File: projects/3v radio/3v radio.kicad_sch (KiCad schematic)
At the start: 6 parts

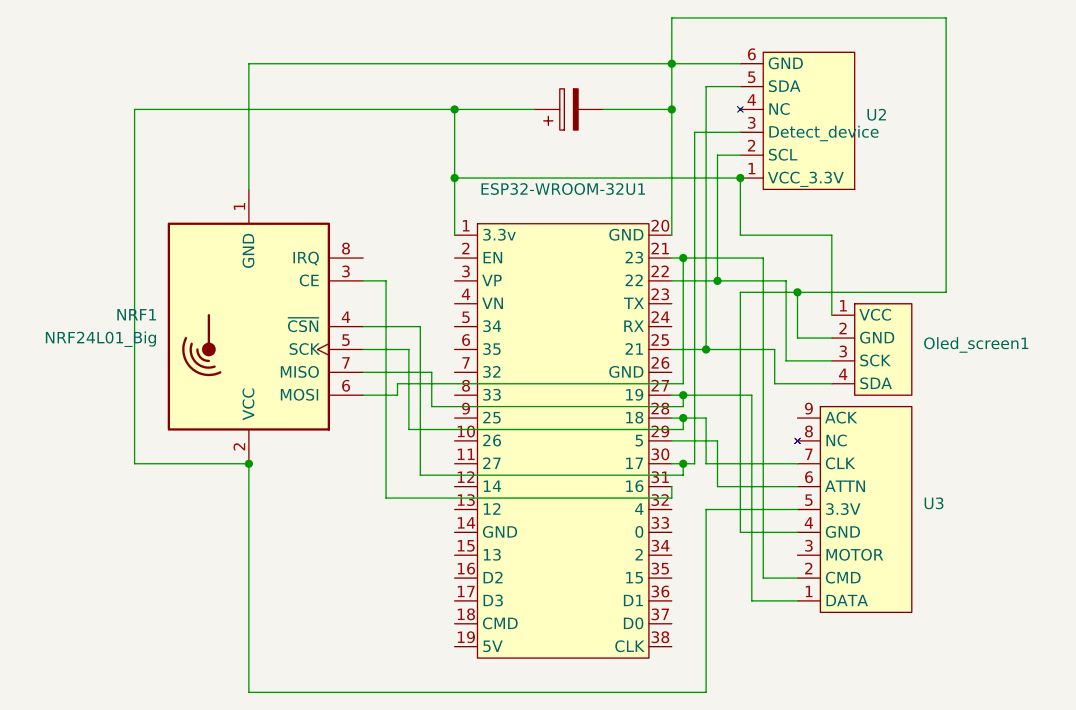
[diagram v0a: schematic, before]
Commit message: 3v rad update
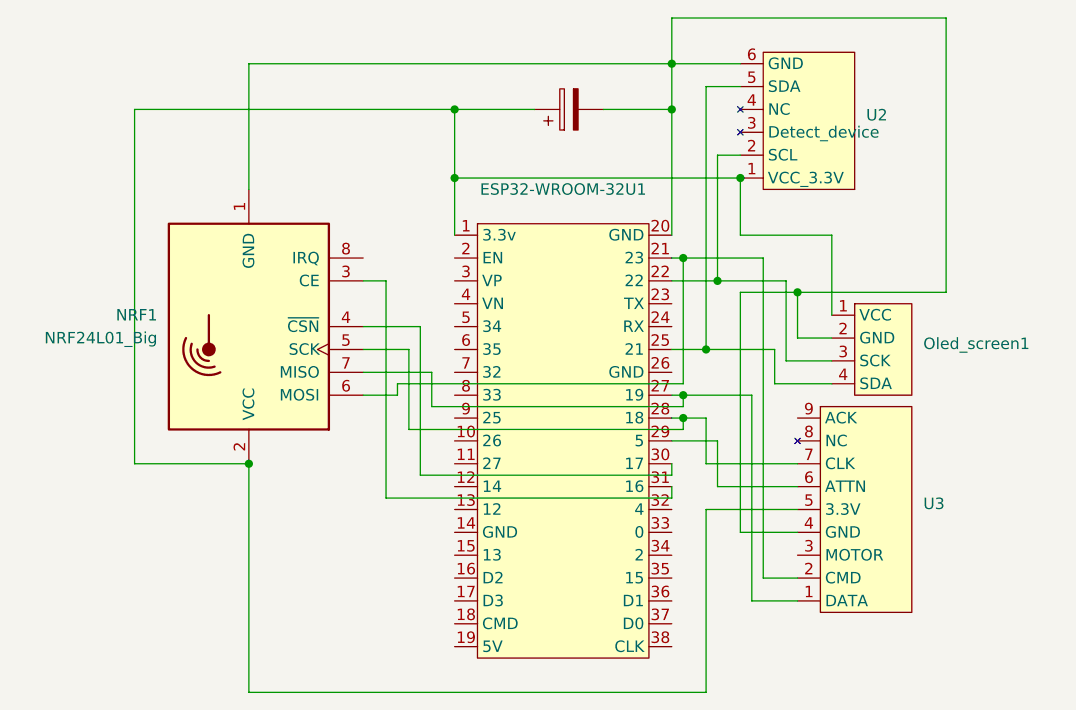
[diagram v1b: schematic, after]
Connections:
- net at ESP32-WROOM-32U1.30 (17), NRF1.4 (~{CSN}): no longer U2.3 (Detect_device)
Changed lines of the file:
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@@
 		(color 0 0 0 0)
 	)
-	(junction
-		(at 148.59 82.55)
-		(diameter 0)
-		(color 0 0 0 0)
-	)
 	(wire
 		(pts
@@
 	(wire
 		(pts
-			(xy 149.86 82.55) (xy 148.59 82.55)
-		)
-		(stroke
-			(width 0)
-			(type default)
-		)
-	)
-	(wire
-		(pts
-			(xy 119.38 83.82) (xy 148.59 83.82)
+			(xy 119.38 83.82) (xy 147.32 83.82)
 		)
 		(stroke
@@
 	(wire
 		(pts
-			(xy 154.94 45.72) (xy 149.86 45.72)
-		)
-		(stroke
-			(width 0)
-			(type default)
-		)
-	)
-	(wire
-		(pts
 			(xy 147.32 57.15) (xy 147.32 43.18)
 		)
@@
 	(wire
 		(pts
-			(xy 149.86 45.72) (xy 149.86 82.55)
-		)
-		(stroke
-			(width 0)
-			(type default)
-		)
-	)
-	(wire
-		(pts
 			(xy 161.29 95.25) (xy 157.48 95.25)
 		)
@@
 	(wire
 		(pts
-			(xy 148.59 82.55) (xy 147.32 82.55)
-		)
-		(stroke
-			(width 0)
-			(type default)
-		)
-	)
-	(wire
-		(pts
 			(xy 115.57 86.36) (xy 147.32 86.36)
 		)
@@
 	(wire
 		(pts
-			(xy 148.59 83.82) (xy 148.59 82.55)
-		)
-		(stroke
+			(xy 147.32 83.82) (xy 147.32 82.55)
+		)
+		(stroke
